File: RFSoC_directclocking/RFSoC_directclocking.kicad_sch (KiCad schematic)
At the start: 15 parts, among them J1 Conn_Coaxial, J2 Conn_Coaxial, J3 Conn_Coaxial, J4 Conn_Coaxial, J5 Conn_Coaxial, U1 TCM2-33WX+, U2 TCM2-33WX+

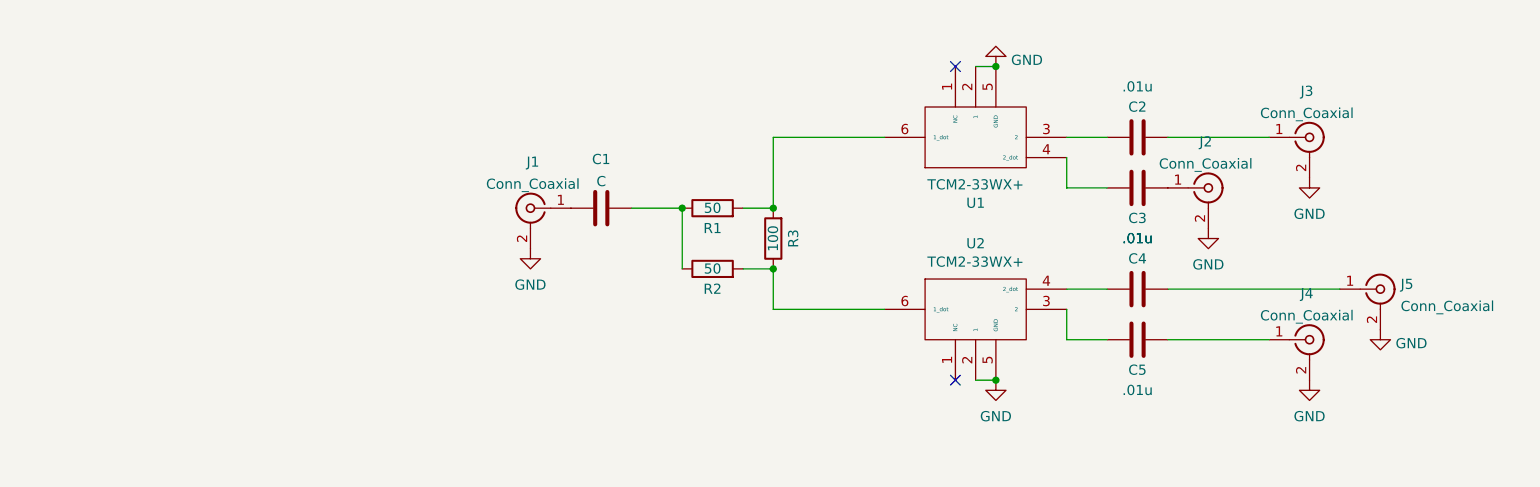
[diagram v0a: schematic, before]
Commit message: added kicad symbol+footprint
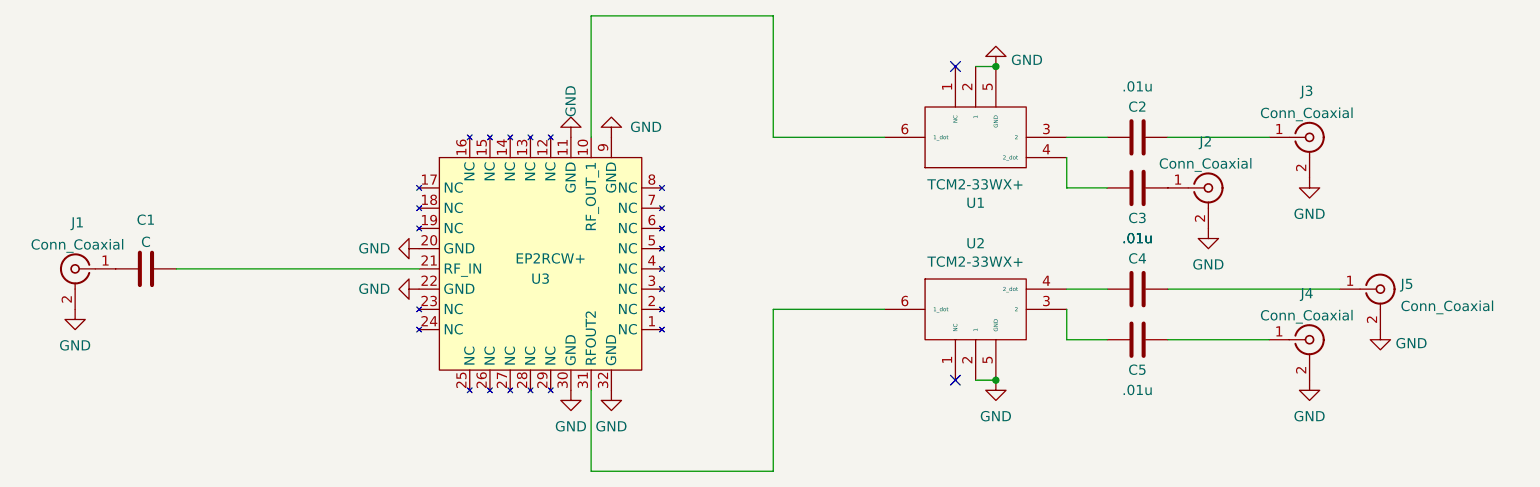
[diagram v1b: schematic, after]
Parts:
- removed R1, R2: 50, Resistor_SMD:R_0402_1005Metric, symbol Device:R
- removed R3: 100, Resistor_SMD:R_0402_1005Metric, symbol Device:R
- added U3: EP2RCW+, Mouser:QFN50P500X500X100-33N-D, symbol Power Splitter:EP2RCW+
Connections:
- net GND: now also U3.11 (GND), U3.20 (GND), U3.22 (GND), U3.30 (GND), U3.32 (GND), U3.9 (GND)
- net at C1.2: now also U3.21 (RF_IN)
- net at U1.6 (1_dot): now also U3.10 (RF_OUT_1)
- net at U2.6 (1_dot): now also U3.31 (RFOUT2)
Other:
- moved on the sheet: C1, J1

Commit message: improvements
Made improvement to kicad symbol and replaced footprint for baluns. They
were incorrectly orientated with regards to pin numbering
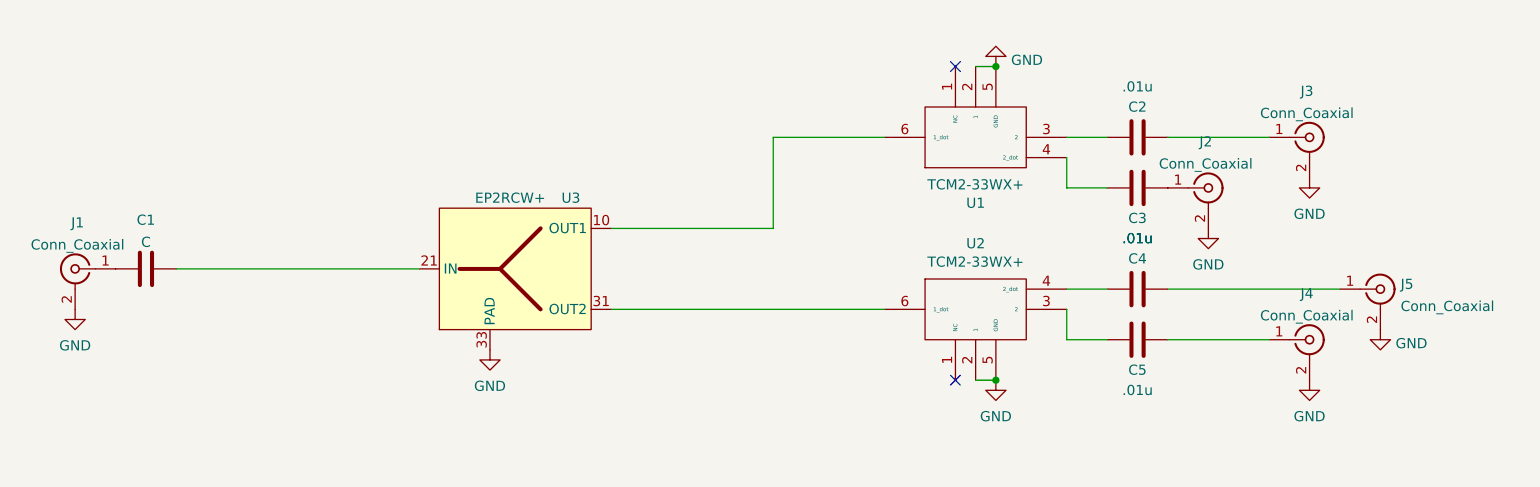
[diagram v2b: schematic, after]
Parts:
- U3: footprint Mouser:QFN50P500X500X100-33N-D -> RF_Mini-Circuits:Mini-Circuits_QQQ130_LandPattern_PL-236_ClockwisePinNumbering; symbol Power Splitter:EP2RCW+ -> Power Splitter:EP2RCW; Part Number EP2RCW -> EP2RCW+
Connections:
- net GND: now also U3.1 (NC), U3.12 (NC), U3.13 (NC), U3.14 (NC), U3.15 (NC), U3.16 (NC), U3.17 (NC), U3.18 (NC), U3.19 (NC), U3.2 (NC), U3.23 (NC), U3.24 (NC), U3.25 (NC), U3.26 (NC), U3.27 (NC), U3.28 (NC), U3.29 (NC), U3.3 (NC), U3.33 (PAD), U3.4 (NC), U3.5 (NC), U3.6 (NC), U3.7 (NC), U3.8 (NC)
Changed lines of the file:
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@@
-    (stroke (width 0) (type default) (color 0 0 0 0))
-  )
-  (wire (pts (xy 121.92 58.42) (xy 121.92 73.66))
     (stroke (width 0) (type default) (color 0 0 0 0))
   )
@@
     (stroke (width 0) (type default) (color 0 0 0 0))
   )
-  (wire (pts (xy 99.06 58.42) (xy 121.92 58.42))
-    (stroke (width 0) (type default) (color 0 0 0 0))
-  )
-  (wire (pts (xy 99.06 73.66) (xy 99.06 58.42))
+  (wire (pts (xy 121.92 85.09) (xy 101.6 85.09))
     (stroke (width 0) (type default) (color 0 0 0 0))
   )
@@
     (stroke (width 0) (type default) (color 0 0 0 0))
   )
-  (wire (pts (xy 121.92 95.25) (xy 135.89 95.25))
-    (stroke (width 0) (type default) (color 0 0 0 0))
-  )
-  (wire (pts (xy 99.06 105.41) (xy 99.06 115.57))
-    (stroke (width 0) (type default) (color 0 0 0 0))
-  )
-  (wire (pts (xy 99.06 115.57) (xy 121.92 115.57))
-    (stroke (width 0) (type default) (color 0 0 0 0))
-  )
-  (wire (pts (xy 121.92 115.57) (xy 121.92 95.25))
+  (wire (pts (xy 101.6 95.25) (xy 135.89 95.25))
+    (stroke (width 0) (type default) (color 0 0 0 0))
+  )
+  (wire (pts (xy 121.92 73.66) (xy 121.92 85.09))
     (stroke (width 0) (type default) (color 0 0 0 0))
   )
@@
     (pin "2")
   )
-  (symbol (lib_id "power:GND") (at 101.6 73.66 0) (mirror x) (unit 1)
-    (in_bom yes) (on_board yes)
-    (property "Reference" "#PWR0105" (id 0) (at 101.6 67.31 0)
-      (effects (font (size 1.27 1.27)) hide)
-    )
-    (property "Value" "GND" (id 1) (at 107.95 72.39 0)
-      (effects (font (size 1.27 1.27)) (justify right))
-    )
-    (property "Footprint" "" (id 2) (at 101.6 73.66 0)
-      (effects (font (size 1.27 1.27)) hide)
-    )
-    (property "Datasheet" "" (id 3) (at 101.6 73.66 0)
-      (effects (font (size 1.27 1.27)) hide)
-    )
-    (pin "1")
-  )
-  (symbol (lib_id "Power Splitter:EP2RCW+") (at 92.71 88.9 270) (unit 1)
-    (in_bom yes) (on_board yes)
-    (property "Reference" "U3" (id 0) (at 92.71 91.44 90))
-    (property "Value" "EP2RCW+" (id 1) (at 93.98 88.9 90))
-    (property "Footprint" "Mouser:QFN50P500X500X100-33N-D" (id 2) (at 106.68 63.5 0)
-      (effects (font (size 1.27 1.27)) hide)
-    )
-    (property "Datasheet" "https://www.minicircuits.com/WebStore/dashboardPdf?model=EP2RCW%2B" (id 3) (at 106.68 63.5 0)
-      (effects (font (size 1.27 1.27)) hide)
-    )
-    (property "Part Number" "EP2RCW" (id 4) (at 92.71 88.9 90)
-      (effects (font (size 1.27 1.27)) hide)
-    )
-    (property "Link" "https://www.mouser.com/ProductDetail/Mini-Circuits/EP2RCW%2b?qs=7MVldsJ5UawdT%252BMSbph5ew%3D%3D" (id 5) (at 92.71 88.9 90)
+  (symbol (lib_id "Power Splitter:EP2RCW") (at 87.63 90.17 0) (unit 1)
+    (in_bom yes) (on_board yes)
+    (property "Reference" "U3" (id 0) (at 96.52 81.28 0))
+    (property "Value" "EP2RCW+" (id 1) (at 88.9 81.28 0))
+    (property "Footprint" "RF_Mini-Circuits:Mini-Circuits_QQQ130_LandPattern_PL-236_ClockwisePinNumbering" (id 2) (at 88.9 125.73 0)
+      (effects (font (size 1.27 1.27)) hide)
+    )
+    (property "Datasheet" "https://www.minicircuits.com/pdfs/LRPS-2-1.pdf" (id 3) (at 87.63 123.19 0)
+      (effects (font (size 1.27 1.27)) hide)
+    )
+    (property "Part Number" "EP2RCW+" (id 4) (at 81.28 120.65 0)
+      (effects (font (size 1.27 1.27)) hide)
+    )
+    (property "Link" "https://www.mouser.com/ProductDetail/Mini-Circuits/EP2RCW%2b?qs=7MVldsJ5UawdT%252BMSbph5ew%3D%3D" (id 5) (at 87.63 90.17 90)
       (effects (font (size 1.27 1.27)) hide)
     )
@@
     (pin "31")
     (pin "32")
+    (pin "33")
     (pin "4")
     (pin "5")
@@
     (pin "1")
   )
-  (symbol (lib_id "power:GND") (at 101.6 105.41 0) (mirror y) (unit 1)
-    (in_bom yes) (on_board yes) (fields_autoplaced)
-    (property "Reference" "#PWR0101" (id 0) (at 101.6 111.76 0)
-      (effects (font (size 1.27 1.27)) hide)
-    )
-    (property "Value" "GND" (id 1) (at 101.6 109.9725 0))
-    (property "Footprint" "" (id 2) (at 101.6 105.41 0)
-      (effects (font (size 1.27 1.27)) hide)
-    )
-    (property "Datasheet" "" (id 3) (at 101.6 105.41 0)
-      (effects (font (size 1.27 1.27)) hide)
-    )
-    (pin "1")
-  )
-  (symbol (lib_id "power:GND") (at 77.47 92.71 270) (mirror x) (unit 1)
-    (in_bom yes) (on_board yes)
-    (property "Reference" "#PWR0104" (id 0) (at 71.12 92.71 0)
-      (effects (font (size 1.27 1.27)) hide)
-    )
-    (property "Value" "GND" (id 1) (at 69.85 92.71 90)
-      (effects (font (size 1.27 1.27)) (justify left))
-    )
-    (property "Footprint" "" (id 2) (at 77.47 92.71 0)
-      (effects (font (size 1.27 1.27)) hide)
-    )
-    (property "Datasheet" "" (id 3) (at 77.47 92.71 0)
-      (effects (font (size 1.27 1.27)) hide)
-    )
-    (pin "1")
-  )
   (symbol (lib_id "power:GND") (at 198.12 97.79 0) (unit 1)
     (in_bom yes) (on_board yes) (fields_autoplaced)
@@
     (pin "1")
     (pin "2")
-  )
-  (symbol (lib_id "power:GND") (at 96.52 73.66 0) (mirror x) (unit 1)
-    (in_bom yes) (on_board yes)
-    (property "Reference" "#PWR0106" (id 0) (at 96.52 67.31 0)
-      (effects (font (size 1.27 1.27)) hide)
-    )
-    (property "Value" "GND" (id 1) (at 96.52 71.12 90)
-      (effects (font (size 1.27 1.27)) (justify right))
-    )
-    (property "Footprint" "" (id 2) (at 96.52 73.66 0)
-      (effects (font (size 1.27 1.27)) hide)
-    )
-    (property "Datasheet" "" (id 3) (at 96.52 73.66 0)
-      (effects (font (size 1.27 1.27)) hide)
-    )
-    (pin "1")
   )
   (symbol (lib_id "power:GND") (at 189.23 78.74 0) (mirror y) (unit 1)
@@
     (pin "1")
   )
-  (symbol (lib_id "power:GND") (at 96.52 105.41 0) (mirror y) (unit 1)
-    (in_bom yes) (on_board yes) (fields_autoplaced)
-    (property "Reference" "#PWR0102" (id 0) (at 96.52 111.76 0)
-      (effects (font (size 1.27 1.27)) hide)
-    )
-    (property "Value" "GND" (id 1) (at 96.52 109.9725 0))
-    (property "Footprint" "" (id 2) (at 96.52 105.41 0)
-      (effects (font (size 1.27 1.27)) hide)
-    )
-    (property "Datasheet" "" (id 3) (at 96.52 105.41 0)
+  (symbol (lib_id "power:GND") (at 86.36 100.33 0) (mirror y) (unit 1)
+    (in_bom yes) (on_board yes) (fields_autoplaced)
+    (property "Reference" "#PWR0102" (id 0) (at 86.36 106.68 0)
+      (effects (font (size 1.27 1.27)) hide)
+    )
+    (property "Value" "GND" (id 1) (at 86.36 104.8925 0))
+    (property "Footprint" "" (id 2) (at 86.36 100.33 0)
+      (effects (font (size 1.27 1.27)) hide)
+    )
+    (property "Datasheet" "" (id 3) (at 86.36 100.33 0)
       (effects (font (size 1.27 1.27)) hide)
     )
@@
     (pin "2")
   )
-  (symbol (lib_id "power:GND") (at 77.47 87.63 270) (mirror x) (unit 1)
-    (in_bom yes) (on_board yes)
-    (property "Reference" "#PWR0103" (id 0) (at 71.12 87.63 0)
-      (effects (font (size 1.27 1.27)) hide)
-    )
-    (property "Value" "GND" (id 1) (at 69.85 87.63 90)
-      (effects (font (size 1.27 1.27)) (justify left))
-    )
-    (property "Footprint" "" (id 2) (at 77.47 87.63 0)
-      (effects (font (size 1.27 1.27)) hide)
-    )
-    (property "Datasheet" "" (id 3) (at 77.47 87.63 0)
-      (effects (font (size 1.27 1.27)) hide)
-    )
-    (pin "1")
-  )
   (symbol (lib_id "power:GND") (at 149.86 104.14 0) (unit 1)
     (in_bom yes) (on_board yes) (fields_autoplaced)
@@
       (reference "#PWR07") (unit 1) (value "GND") (footprint "")
     )
-    (path "/595efaee-6b86-4c6a-afdf-efc352080aba"
-      (reference "#PWR0101") (unit 1) (value "GND") (footprint "")
-    )
     (path "/afc0baca-f312-432e-a9ff-002564fdbca1"
       (reference "#PWR0102") (unit 1) (value "GND") (footprint "")
     )
-    (path "/ee84f8f8-deb8-4a94-9089-f58240794eed"
-      (reference "#PWR0103") (unit 1) (value "GND") (footprint "")
-    )
-    (path "/5aded1f4-2d79-43da-8261-87633a3461cb"
-      (reference "#PWR0104") (unit 1) (value "GND") (footprint "")
-    )
-    (path "/366b2aa3-82f4-4959-8f38-a725c41de028"
-      (reference "#PWR0105") (unit 1) (value "GND") (footprint "")
-    )
-    (path "/692eaaff-ab2c-4dca-b4b0-f62da3eb7ffd"
-      (reference "#PWR0106") (unit 1) (value "GND") (footprint "")
-    )
     (path "/eb978cc2-8d10-4806-86dd-9b56521bf4c2"
       (reference "C1") (unit 1) (value "C") (footprint "Capacitor_SMD:C_0402_1005Metric")
@@
     )
     (path "/4adc3b23-4dc8-43e1-917a-b43db5f55a49"
-      (reference "U3") (unit 1) (value "EP2RCW+") (footprint "Mouser:QFN50P500X500X100-33N-D")
-    )
-  )
+      (reference "U3") (unit 1) (value "EP2RCW+") (footprint "RF_Mini-Circuits:Mini-Circuits_QQQ130_LandPattern_PL-236_ClockwisePinNumbering")
+    )
+  )
